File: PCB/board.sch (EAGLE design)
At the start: 13 parts, among them IC1 W25Q32JVSSIQ, J1 USB-TYPE-C-31-M-17, U1 ESP8266EX, U2 AMS1117_SOT223, Y2 CRYSTAL-26MHZ

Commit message: schematics
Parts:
- removed Y2: CRYSTAL-26MHZ, angrypig7-Clocks:CRYSTAL-26MHZ
- added C10: 100nF, angrypig7-RCL:C-NON-POLC0402
- added C11, C12: 1uF, angrypig7-RCL:C-NON-POLC0402
- added C13: 10uF, angrypig7-RCL:C-NON-POLC0402
- added C14: 5.6pF, angrypig7-RCL:C-NON-POLC0402
- added C8: 20pF, angrypig7-RCL:C-NON-POLC0402
- added R1: (no value), angrypig7-RCL:RR0402
- added R2: 12k, angrypig7-RCL:RR0402
- added U3: ESP01_PINOUT, angrypig7-IC:ESP01_PINOUT
- added X1: SMA, angrypig7-Connectors:SMA_END-LAUNCH-1
- added Y1: 26Mhz, angrypig7-Clocks:CRYSTAL-26MHZ
- C9: value 1uF -> 20pF; LCSC C52923 -> C1554
- U2: LCSC (none) -> C6186
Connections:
- new net ADC_IN: U1.TOUT
- new net CHIP_EN: U1.CHIP_EN, U3.CH_PD
- new net GPIO0: U1.GPIO0, U3.GPIO0
- new net GPIO12: U1.MTDI
- new net GPIO13: U1.MTCK
- new net GPIO14: U1.MTMS
- new net GPIO15: U1.MTDO
- new net GPIO16: U1.XPD_DCDC
- new net GPIO2: U1.GPIO2, U3.GPIO2
- new net GPIO4: U1.GPIO4
- new net GPIO5: U1.GPIO5
- new net N$1: C9.2, U1.XTAL_IN, Y1.2
- new net N$2: C8.2, U1.XTAL_OUT, Y1.1
- new net N$3: R1.1, U1.SD_CLK
- new net N$4: R2.2, U1.RES12K
- new net N$5: U1.LNA
- new net N$6: X1.1
- new net RST: U1.EXT_RSTB, U3.RST
- new net SD_CLK: IC1.CLK, R1.2
- new net SD_CMD: IC1./CS, U1.SD_CMD
- new net SD_D0: IC1.DO(IO1), U1.SD_DATA_0
- new net SD_D1: IC1.DI(IO0), U1.SD_DATA_1
- new net SD_D2: IC1.IO3, U1.SD_DATA_2
- new net SD_D3: IC1.IO2, U1.SD_DATA_3
- new net URXD: U1.U0RXD, U3.RXD
- new net UTXD: U1.U0TXD, U3.TXD
- net 3.3V: now also C10.1, C11.1, C12.1, C13.1, U1.VDD3P3, U1.VDD3P3$2, U1.VDDPST, U1.VDDPST$2, U3.VCC; no longer C9.1
- net GND: now also C10.2, C11.2, C12.2, C13.2, C8.1, C9.1, R2.1, U3.GND, X1.2, Y1.GND; no longer C9.2
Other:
- moved on the sheet: C6, C7, C9

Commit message: added peripherals
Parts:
- removed C1: 1uF, angrypig7-RCL:C-NON-POLC0402
- added C15: 1uF, angrypig7-RCL:C-NON-POLC0402
- added D1: LED_0603, angrypig7-Diodes:LED_0603
- added R3, R4: 10k, angrypig7-RCL:RR0402
- added S1: RST, angrypig7-Switches:SWITCH-SPST-SMD-6.0X3.5MM
- added S2: FLASH, angrypig7-Switches:SWITCH-SPST-SMD-6.0X3.5MM
- added TP1: TEST-POINT-3, angrypig7-Tests:TEST-POINT-3
- C10: LCSC C52923 -> C1525
- C14: LCSC (none) -> C318596
- R1: value (none) -> 200R; LCSC (none) -> C25087
- X1: LCSC (none) -> C496550
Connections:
- new net N$7: D1.A, R4.1
- net 3.3V: now also C15.1, R3.1, R4.2, TP1.2
- net 5V: now also TP1.3; no longer C1.1
- net CHIP_EN: now also R3.2, S1.1
- net GND: now also C15.2, D1.C, S1.2, S2.2, TP1.1; no longer C1.2
- net GPIO0: now also S2.1
- net N$5: now also C14.1
- net N$6: now also C14.2
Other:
- moved on the sheet: U3

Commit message: PCB layout
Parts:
- removed C15: 1uF, angrypig7-RCL:C-NON-POLC0402
- removed C9: 20pF, angrypig7-RCL:C-NON-POLC0402
- added C1: 1uF, angrypig7-RCL:C-NON-POLC0402
- added JP1: (no value), pinhead_v2:PINHD-1X4/OCT
- C10: value 100nF -> 1uF; LCSC C1525 -> C52923
- C11, C12: value 1uF -> 20pF; LCSC C52923 -> C1554
- C13: value 10uF -> 1uF; LCSC C15525 -> C52923
- C14: value 5.6pF -> 1uF; LCSC C318596 -> C52923
- C2: value 1uF -> 10uF; LCSC C52923 -> C15525
- C3: value 10uF -> 5.6pF; LCSC C15525 -> C318596
- C5: value 100uF -> 10uF; device angrypig7-RCL:C-POLARIZEDSMCB -> angrypig7-RCL:C-NON-POLC0402; LCSC C16133 -> C15525
- C6: value 1uF -> 100uF; device angrypig7-RCL:C-NON-POLC0402 -> angrypig7-RCL:C-POLARIZEDSMCB; LCSC C52923 -> C16133
- C7: value 1uF -> 100nF; LCSC C52923 -> C1525
- C8: value 20pF -> 1uF; LCSC C1554 -> C52923
- D1: LCSC (none) -> C72038
- R1: value 200R -> 10k; LCSC C25087 -> C25744
- R2: value 12k -> 10k; LCSC (none) -> C25744
- R3: value 10k -> 12k; LCSC C25744 -> (none)
- R4: value 10k -> 200R; LCSC C25744 -> C25087
- U1: value ESP8266EX -> ESP01_PINOUT; device angrypig7-IC:ESP8266EX -> angrypig7-IC:ESP01_PINOUT; LCSC C77967 -> (none)
- U3: value ESP01_PINOUT -> ESP8266EX; device angrypig7-IC:ESP01_PINOUT -> angrypig7-IC:ESP8266EX; LCSC (none) -> C77967
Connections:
- net 3.3V: now also C14.1, C2.1, C5.1, C6.+, C8.1, JP1.4, R1.2, R2.1, U1.VCC, U3.VDD3P3, U3.VDD3P3$2, U3.VDDA, U3.VDDA$2, U3.VDDD, U3.VDDPST, U3.VDDPST$2; no longer C11.1, C12.1, C15.1, C3.1, C5.+, C6.1, R3.1, R4.2, U1.VDD3P3, U1.VDD3P3$2, U1.VDDA, U1.VDDA$2, U1.VDDD, U1.VDDPST, U1.VDDPST$2, U3.VCC
- net 5V: now also C1.1; no longer C2.1
- net ADC_IN: now also U3.TOUT; no longer U1.TOUT
- net CHIP_EN: now also R2.2, U1.CH_PD, U3.CHIP_EN; no longer R3.2, U1.CHIP_EN, U3.CH_PD
- net GND: now also C1.2, C11.1, C12.1, C14.2, C5.2, C6.-, C8.2, JP1.1, R3.1; no longer C11.2, C12.2, C15.2, C3.2, C5.-, C6.2, C8.1, C9.1, R2.1
- net GPIO12: now also U3.MTDI; no longer U1.MTDI
- net GPIO13: now also U3.MTCK; no longer U1.MTCK
- net GPIO14: now also U3.MTMS; no longer U1.MTMS
- net GPIO15: now also U3.MTDO; no longer U1.MTDO
- net GPIO16: now also U3.XPD_DCDC; no longer U1.XPD_DCDC
- net GPIO4: now also U3.GPIO4; no longer U1.GPIO4
- net GPIO5: now also U3.GPIO5; no longer U1.GPIO5
- net N$1: now also C12.2, U3.XTAL_IN; no longer C9.2, U1.XTAL_IN
- net N$2: now also C11.2, U3.XTAL_OUT; no longer C8.2, U1.XTAL_OUT
- net N$3: now also R4.1, U3.SD_CLK; no longer R1.1, U1.SD_CLK
- net N$4: now also R3.2, U3.RES12K; no longer R2.2, U1.RES12K
- net N$5: now also C3.1, U3.LNA; no longer C14.1, U1.LNA
- net N$6: now also C3.2; no longer C14.2
- net N$7: now also R1.1; no longer R4.1
- net RST: now also U1.RST, U3.EXT_RSTB; no longer U1.EXT_RSTB, U3.RST
- net SD_CLK: now also R4.2; no longer R1.2
- net SD_CMD: now also U3.SD_CMD; no longer U1.SD_CMD
- net SD_D0: now also U3.SD_DATA_0; no longer U1.SD_DATA_0
- net SD_D1: now also U3.SD_DATA_1; no longer U1.SD_DATA_1
- net SD_D2: now also U3.SD_DATA_2; no longer U1.SD_DATA_2
- net SD_D3: now also U3.SD_DATA_3; no longer U1.SD_DATA_3
- net URXD: now also JP1.3, U1.RXD, U3.U0RXD; no longer U1.U0RXD, U3.RXD
- net UTXD: now also JP1.2, U1.TXD, U3.U0TXD; no longer U1.U0TXD, U3.TXD
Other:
- moved on the sheet: C10, C11, C12, C13, C14, C2, C3, C7, C8, R1, R2, R3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

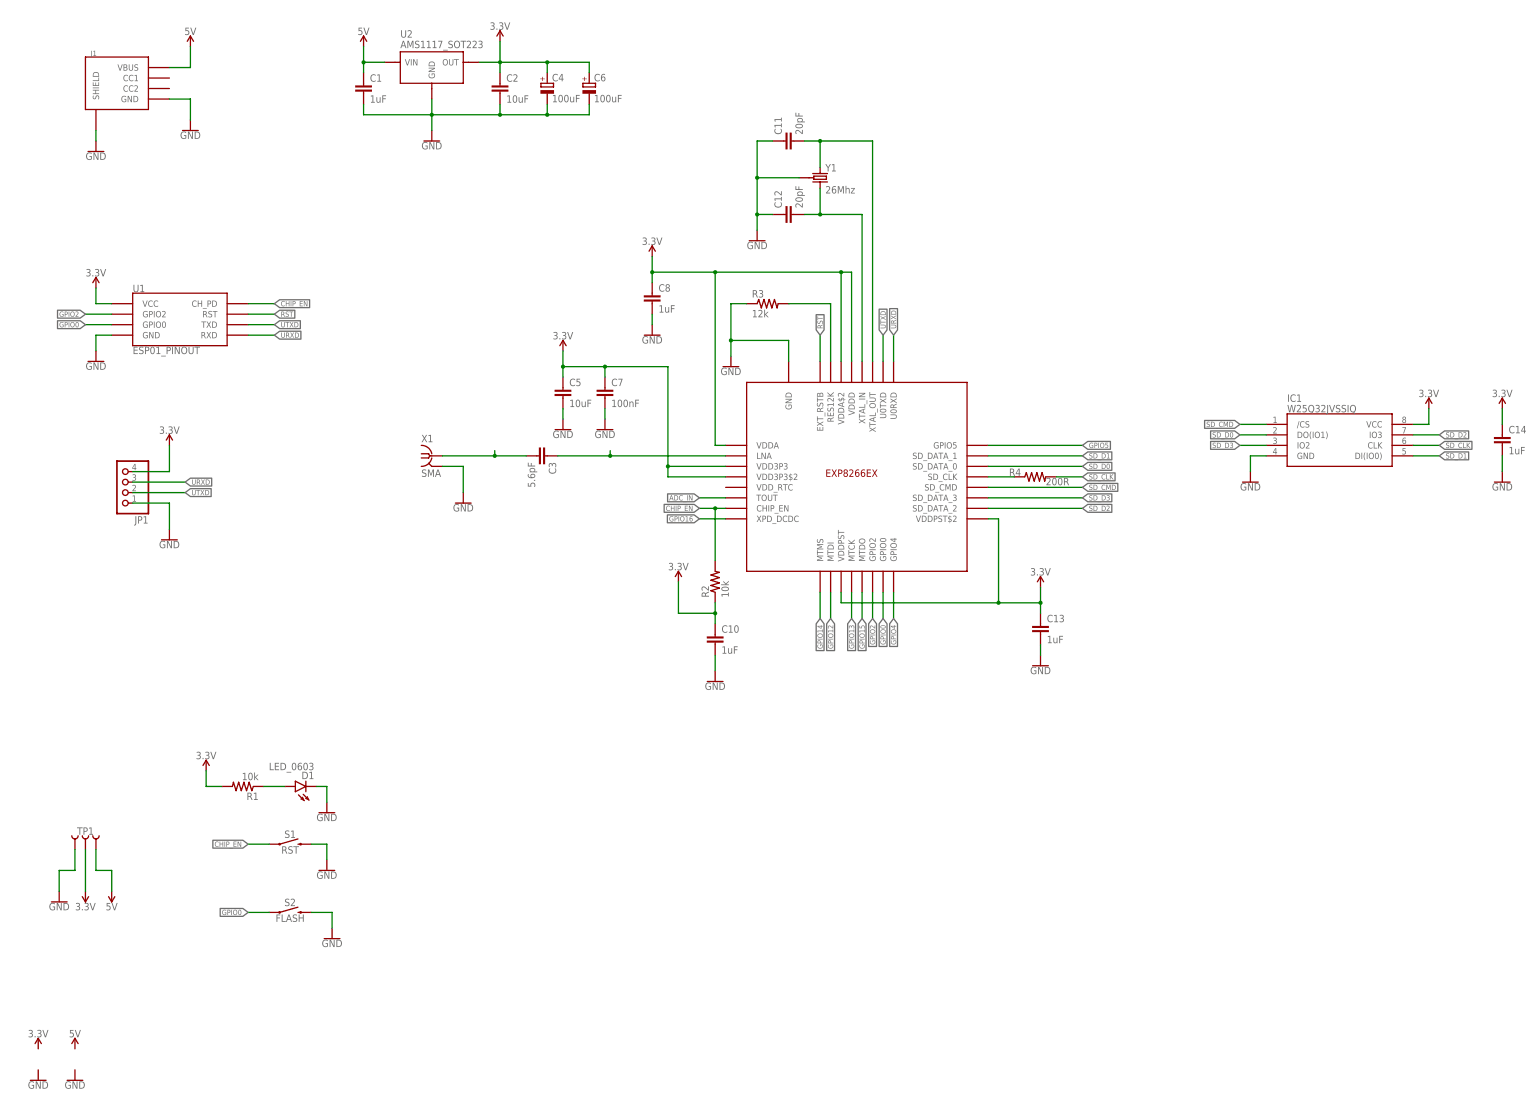
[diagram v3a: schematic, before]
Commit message: added CH340
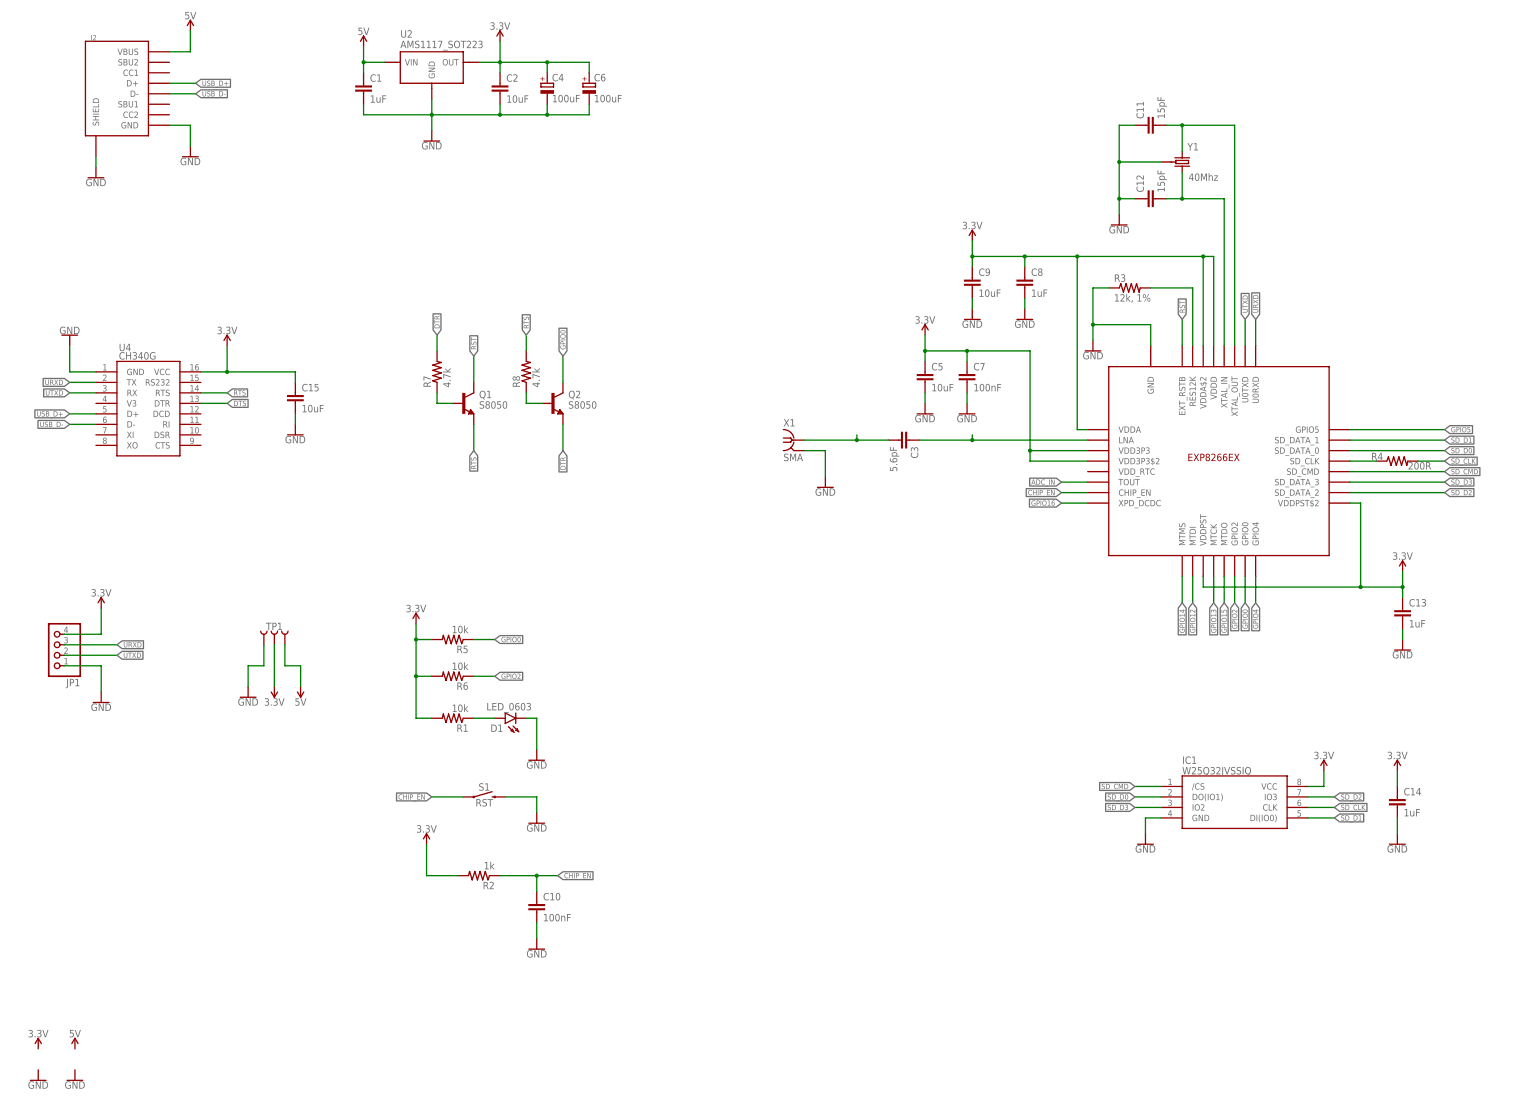
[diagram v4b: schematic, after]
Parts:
- removed J1: USB-TYPE-C-31-M-17, angrypig7-Connectors:USB-TYPE-C-31-M-17
- removed S2: FLASH, angrypig7-Switches:SWITCH-SPST-SMD-6.0X3.5MM
- removed U1: ESP01_PINOUT, angrypig7-IC:ESP01_PINOUT
- added C15, C9: 10uF, angrypig7-RCL:C-NON-POLC0402
- added J2: USB-TYPE-C-31-M-12, angrypig7-Connectors:USB-TYPE-C-31-M-12
- added Q1, Q2: S8050, angrypig7-Transistors:S8050
- added R5, R6: 10k, angrypig7-RCL:RR0402
- added R7, R8: 4.7k, angrypig7-RCL:RR0402
- added U4: CH340G, angrypig7-IC:CH340G
- C10: value 1uF -> 100nF; LCSC C52923 -> C1525
- C11, C12: value 20pF -> 15pF; LCSC C1554 -> C1548
- R2: value 10k -> 1k; LCSC C25744 -> C11702
- R3: value 12k -> 12k, 1%; LCSC (none) -> C25752
- Y1: value 26Mhz -> 40Mhz; device angrypig7-Clocks:CRYSTAL-26MHZ -> angrypig7-Clocks:CRYSTAL-40MHZ_2520; LCSC C91747 -> C284176
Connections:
- new net DTR: Q2.E, R7.2
- new net DTS: U4.DTR
- new net N$8: Q1.B, R7.1
- new net N$9: Q2.B, R8.1
- new net RTS: Q1.E, R8.2, U4.RTS
- new net USB_D+: J2.D+, U4.D+
- new net USB_D-: J2.D-, U4.D-
- net 3.3V: now also C15.1, C9.1, R2.2, R5.2, R6.2, U4.VCC; no longer C10.1, R2.1, U1.VCC
- net 5V: now also J2.VBUS; no longer J1.VBUS
- net CHIP_EN: now also C10.1, R2.1; no longer R2.2, U1.CH_PD
- net GND: now also C15.2, C9.2, J2.GND, J2.SHIELD, U4.GND; no longer J1.GND, J1.SHIELD, S2.2, U1.GND
- net GPIO0: now also Q2.C, R5.1; no longer S2.1, U1.GPIO0
- net GPIO2: now also R6.1; no longer U1.GPIO2
- net RST: now also Q1.C; no longer U1.RST
- net URXD: now also U4.TX; no longer U1.RXD
- net UTXD: now also U4.RX; no longer U1.TXD
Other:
- moved on the sheet: C10, C11, C12, C13, C14, C3, C5, C7, C8, D1, IC1, JP1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

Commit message: first version, added gerbers and BOM
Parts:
- removed U4: CH340G, angrypig7-IC:CH340G
- added C16: 100uF, angrypig7-RCL:C-POLARIZEDSMCB
- added U1: AMS1117_SOT223, angrypig7-IC-Power:AMS1117_SOT223
- C11: value 15pF -> 10uF; LCSC C1548 -> C15525
- C12: value 15pF -> 5.6pF; LCSC C1548 -> C318596
- C15: value 10uF -> 100nF; LCSC C15525 -> C1525
- C3: value 5.6pF -> 100uF; device angrypig7-RCL:C-NON-POLC0402 -> angrypig7-RCL:C-POLARIZEDSMCB; LCSC C318596 -> C16133
- C5: value 10uF -> 15pF; LCSC C15525 -> C1548
- C6: value 100uF -> 15pF; device angrypig7-RCL:C-POLARIZEDSMCB -> angrypig7-RCL:C-NON-POLC0402; LCSC C16133 -> C1548
- C7: value 100nF -> 10uF; LCSC C1525 -> C15525
- R1: value 10k -> 12k,1%; LCSC C25744 -> C25752
- R2: value 1k -> 4.7k; LCSC C11702 -> C25900
- R3: value 12k, 1% -> 4.7k; LCSC C25752 -> C25900
- R7: value 4.7k -> 10k; LCSC C25900 -> C25744
- R8: value 4.7k -> 1k; LCSC C25900 -> C11702
- U2: value AMS1117_SOT223 -> CH340G; device angrypig7-IC-Power:AMS1117_SOT223 -> angrypig7-IC:CH340G; LCSC C6186 -> C14267
- renumbered J2 to J1
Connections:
- removed net USB_D+: J1.D+, U4.D+
- removed net USB_D-: J1.D-, U4.D-
- new net USB_N: J1.D-, U2.D-
- new net USB_P: J1.D+, U2.D+
- net 3.3V: now also C10.1, C11.1, C16.+, C3.+, R7.2, R8.2, U1.OUT, U2.VCC; no longer C15.1, C5.1, C6.+, R1.2, R2.2, U2.OUT, U4.VCC
- net 5V: now also U1.VIN; no longer U2.VIN
- net CHIP_EN: now also C15.1, R8.1; no longer C10.1, R2.1
- net DTR: now also R2.2; no longer R7.2
- net DTS: now also U2.DTR; no longer U4.DTR
- net GND: now also C11.2, C16.-, C3.-, C5.1, C6.1, R1.1, U1.GND; no longer C11.1, C12.1, C5.2, C6.-, R3.1, U4.GND
- net N$1: now also C6.2; no longer C12.2
- net N$2: now also C5.2; no longer C11.2
- net N$4: now also R1.2; no longer R3.2
- net N$5: now also C12.1; no longer C3.1
- net N$6: now also C12.2; no longer C3.2
- net N$7: now also R7.1; no longer R1.1
- net N$8: now also R2.1; no longer R7.1
- net N$9: now also R3.1; no longer R8.1
- net RTS: now also R3.2, U2.RTS; no longer R8.2, U4.RTS
- net URXD: now also U2.TX; no longer U4.TX
- net UTXD: now also U2.RX; no longer U4.RX
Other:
- moved on the sheet: C10, C11, C12, C15, C4, C5, C7, C9, R1, R2, R3, R7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

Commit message: CH340C
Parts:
- U2: value CH340G -> CH340C; device angrypig7-IC:CH340G -> angrypig7-IC:CH340C
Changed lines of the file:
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@@
 <attribute name="LCSC" value="C25744"/>
 </part>
-<part name="U2" library="angrypig7-IC" deviceset="CH340G" device="">
+<part name="U2" library="angrypig7-IC" deviceset="CH340C" device="">
 <attribute name="LCSC" value="C14267"/>
 </part>
@@
 <attribute name="LCSC" x="118.11" y="110.49" size="1.27" layer="96" rot="R180" display="off"/>
 </instance>
-<instance part="U2" gate="G$1" x="44.45" y="173.99" smashed="yes">
-<attribute name="NAME" x="37.2872" y="189.1792" size="1.778" layer="95"/>
-<attribute name="VALUE" x="37.2872" y="187.1472" size="1.778" layer="95"/>
-<attribute name="LCSC" x="44.45" y="173.99" size="1.27" layer="96" display="off"/>
+<instance part="U2" gate="G$1" x="44.45" y="175.26" smashed="yes">
+<attribute name="NAME" x="37.2872" y="190.4492" size="1.778" layer="95"/>
+<attribute name="VALUE" x="37.2872" y="188.4172" size="1.778" layer="95"/>
+<attribute name="LCSC" x="44.45" y="175.26" size="1.27" layer="96" display="off"/>
 </instance>
 <instance part="J1" gate="G$1" x="35.56" y="252.73" smashed="yes">

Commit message: CH340C - V3 pin wiring error
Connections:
- net 3.3V: now also U2.V3
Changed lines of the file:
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@@
 <attribute name="LCSC" value="C16133"/>
 </part>
+<part name="SUPPLY6" library="SparkFun-PowerSymbols" deviceset="3.3V" device=""/>
 </parts>
 <sheets>
@@
 <attribute name="VALUE" x="162.433" y="249.4026" size="1.778" layer="96"/>
 <attribute name="LCSC" x="161.29" y="252.73" size="1.778" layer="96" display="off"/>
+</instance>
+<instance part="SUPPLY6" gate="G$1" x="13.97" y="184.15" smashed="yes">
+<attribute name="VALUE" x="13.97" y="186.944" size="1.778" layer="96" align="bottom-center"/>
 </instance>
 </instances>
@@
 <junction x="63.5" y="184.15"/>
 </segment>
+<segment>
+<pinref part="SUPPLY6" gate="G$1" pin="3.3V"/>
+<wire x1="13.97" y1="184.15" x2="13.97" y2="176.53" width="0.1524" layer="91"/>
+<pinref part="U2" gate="G$1" pin="V3"/>
+<wire x1="31.75" y1="176.53" x2="13.97" y2="176.53" width="0.1524" layer="91"/>
+</segment>
 </net>
